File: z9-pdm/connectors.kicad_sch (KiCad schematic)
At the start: 11 parts, among them J10 RedCubeTerminal, J11 RedCubeTerminal, J12 Wago 12 pin 1 level 3.5mm 260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, J13 TE_DT15-12PC-B016 -Conn_01x12, J16 JST GH, J17 Wago 12 pin 1 level 3.5mm 260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, J19 Wago 12 pin 1 level 3.5mm 260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, J2 TE_DT15-12PC-B016 -Conn_01x12, J20 TE_DT15-12PC-B016 -Conn_01x12, J21 Wago 12 pin 1 level 3.5mm 260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

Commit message: x
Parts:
- J16: symbol dnt_global:JST_06 -> dnt_global:Conn_JST_06
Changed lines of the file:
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@@
 	)
 	(symbol
-		(lib_id "dnt_global:JST_06")
+		(lib_id "dnt_global:Conn_JST_06")
 		(at 67.31 167.64 0)
 		(mirror x)

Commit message: x
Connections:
- net HC_1 renamed OUT_HC_1
- net HC_10 renamed OUT_HC_10
- net HC_11 renamed OUT_HC_11
- net HC_12 renamed OUT_HC_12
- net HC_2 renamed OUT_HC_2
- net HC_3 renamed OUT_HC_3
- net HC_4 renamed OUT_HC_4
- net HC_5 renamed OUT_HC_5
- net HC_6 renamed OUT_HC_6
- net HC_7 renamed OUT_HC_7
- net HC_8 renamed OUT_HC_8
- net HC_9 renamed OUT_HC_9
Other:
- moved on the sheet: J12, J13, J19, J20

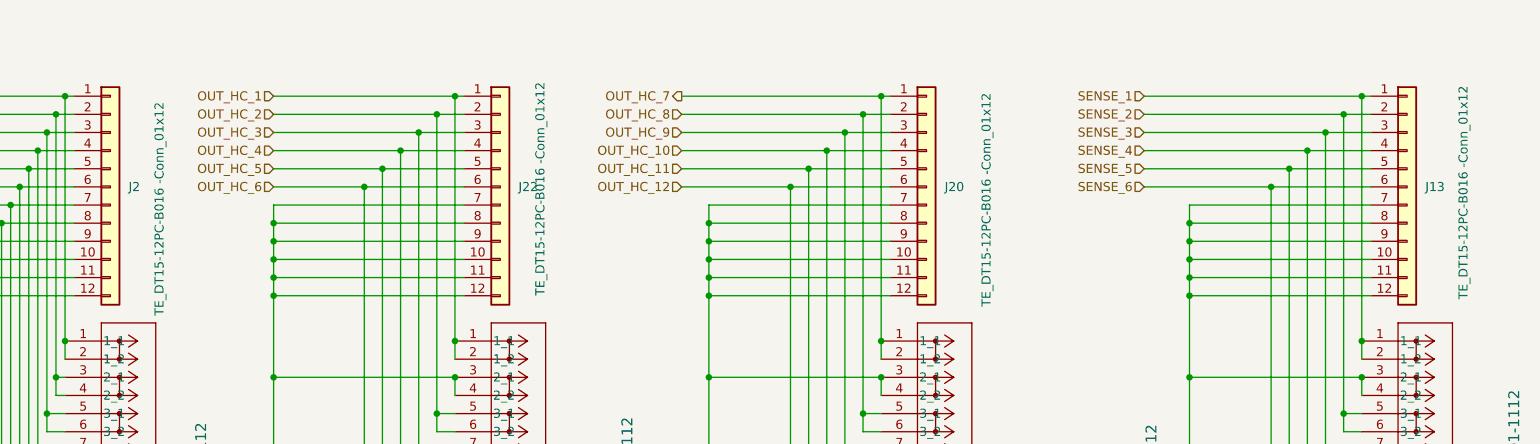
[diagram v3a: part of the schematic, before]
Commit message: lcd power switch-- add new accelerometer
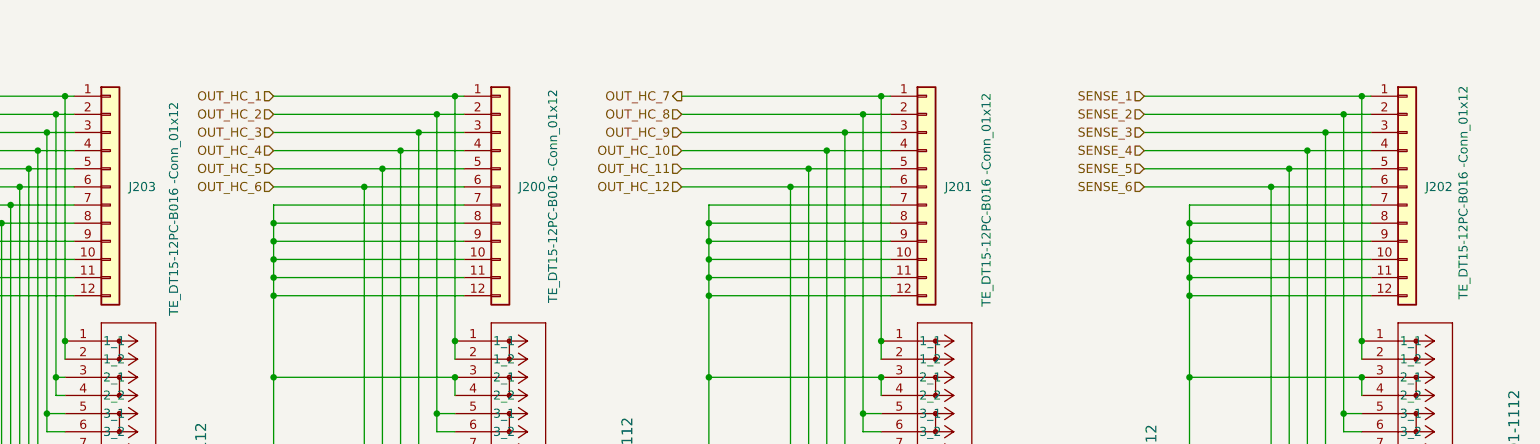
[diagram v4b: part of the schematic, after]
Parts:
- renumbered J22 to J200, J20 to J201, J13 to J202, J2 to J203
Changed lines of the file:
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@@
 		(on_board yes)
 		(dnp no)
-		(property "Reference" "J2"
+		(property "Reference" "J203"
 			(at 83.82 43.1799 0)
 			(effects
@@
 		)
 		(property "Value" "TE_DT15-12PC-B016 -Conn_01x12"
-			(at 88.138 61.214 90)
+			(at 90.17 61.214 90)
 			(effects
 				(font
@@
 			(project "z9-pdm-pcb"
 				(path "/8d063f79-9282-4820-bcf4-1ff3c006cf08/651fe70f-48a4-454d-84e2-56b28624b7c9"
-					(reference "J2")
+					(reference "J203")
 					(unit 1)
 				)
@@
 		(on_board yes)
 		(dnp no)
-		(property "Reference" "J22"
+		(property "Reference" "J200"
 			(at 138.43 43.1799 0)
 			(effects
@@
 		)
 		(property "Value" "TE_DT15-12PC-B016 -Conn_01x12"
-			(at 141.478 58.42 90)
+			(at 143.256 59.436 90)
 			(effects
 				(font
@@
 			(project "z9-pdm-pcb"
 				(path "/8d063f79-9282-4820-bcf4-1ff3c006cf08/651fe70f-48a4-454d-84e2-56b28624b7c9"
-					(reference "J22")
+					(reference "J200")
 					(unit 1)
 				)
@@
 		(on_board yes)
 		(dnp no)
-		(property "Reference" "J20"
+		(property "Reference" "J201"
 			(at 198.12 43.1799 0)
 			(effects
@@
 			(project "z9-pdm-pcb"
 				(path "/8d063f79-9282-4820-bcf4-1ff3c006cf08/651fe70f-48a4-454d-84e2-56b28624b7c9"
-					(reference "J20")
+					(reference "J201")
 					(unit 1)
 				)
@@
 		(on_board yes)
 		(dnp no)
-		(property "Reference" "J13"
+		(property "Reference" "J202"
 			(at 265.43 43.1799 0)
 			(effects
@@
 			(project "z9-pdm-pcb"
 				(path "/8d063f79-9282-4820-bcf4-1ff3c006cf08/651fe70f-48a4-454d-84e2-56b28624b7c9"
-					(reference "J13")
+					(reference "J202")
 					(unit 1)
 				)
